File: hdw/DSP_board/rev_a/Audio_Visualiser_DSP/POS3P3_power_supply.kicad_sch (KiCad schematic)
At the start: 25 parts, among them Q401 BSS214NW, Q402 ZXMS6004FFTA, U401 74LVC1G97, U402 TPS62130A

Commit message: assigned many digi-key part numbers
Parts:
- C401, C406: Digi-Key PN (none) -> 1276-CL05B104KB5NNNCCT-ND
- C402, C404: Digi-Key PN (none) -> 1276-1075-1-ND
- C403, C407, C408: Digi-Key PN (none) -> 490-14381-1-ND
- C405: Digi-Key PN (none) -> 490-4516-1-ND
- R401, R406: Digi-Key PN (none) -> 311-0.0LRCT-ND
- R402, R403, R404: Digi-Key PN (none) -> 311-10.0KLRCT-ND
- R405, R408: Digi-Key PN (none) -> 311-10.0LRCT-ND
- R409: Digi-Key PN (none) -> 311-3.16KLRCT-ND
- R410: Digi-Key PN (none) -> 311-1.00KLRCT-ND
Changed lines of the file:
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@@
 			)
 		)
-		(property "Digi-Key PN" ""
+		(property "Digi-Key PN" "490-14381-1-ND"
 			(at 97.155 153.67 0)
 			(hide yes)
@@
 			)
 		)
-		(property "Digi-Key PN" ""
+		(property "Digi-Key PN" "311-10.0KLRCT-ND"
 			(at 78.74 78.74 0)
 			(hide yes)
@@
 			)
 		)
-		(property "Digi-Key PN" ""
+		(property "Digi-Key PN" "311-1.00KLRCT-ND"
 			(at 214.63 104.14 0)
 			(hide yes)
@@
 			)
 		)
-		(property "Digi-Key PN" ""
+		(property "Digi-Key PN" "311-10.0KLRCT-ND"
 			(at 55.88 104.14 0)
 			(hide yes)
@@
 			)
 		)
-		(property "Digi-Key PN" ""
+		(property "Digi-Key PN" "490-14381-1-ND"
 			(at 200.025 63.5 0)
 			(hide yes)
@@
 			)
 		)
-		(property "Digi-Key PN" ""
+		(property "Digi-Key PN" "311-3.16KLRCT-ND"
 			(at 222.25 88.9 0)
 			(hide yes)
@@
 			)
 		)
-		(property "Digi-Key PN" ""
+		(property "Digi-Key PN" "490-14381-1-ND"
 			(at 184.785 63.5 0)
 			(hide yes)
@@
 			)
 		)
-		(property "Digi-Key PN" ""
+		(property "Digi-Key PN" "1276-CL05B104KB5NNNCCT-ND"
 			(at 67.31 114.3 0)
 			(hide yes)
@@
 			)
 		)
-		(property "Digi-Key PN" ""
+		(property "Digi-Key PN" "1276-1075-1-ND"
 			(at 100.965 55.88 0)
 			(hide yes)
@@
 			)
 		)
-		(property "Digi-Key PN" ""
+		(property "Digi-Key PN" "1276-CL05B104KB5NNNCCT-ND"
 			(at 115.57 68.58 0)
 			(hide yes)
@@
 			)
 		)
-		(property "Digi-Key PN" ""
+		(property "Digi-Key PN" "311-0.0LRCT-ND"
 			(at 43.18 179.07 0)
 			(hide yes)
@@
 			)
 		)
-		(property "Digi-Key PN" ""
+		(property "Digi-Key PN" "1276-1075-1-ND"
 			(at 81.915 55.88 0)
 			(hide yes)
@@
 			)
 		)
-		(property "Digi-Key PN" ""
+		(property "Digi-Key PN" "311-10.0LRCT-ND"
 			(at 189.23 60.96 0)
 			(hide yes)
@@
 			)
 		)
-		(property "Digi-Key PN" ""
+		(property "Digi-Key PN" "311-0.0LRCT-ND"
 			(at 181.61 104.14 0)
 			(hide yes)
@@
 			)
 		)
-		(property "Digi-Key PN" ""
+		(property "Digi-Key PN" "311-10.0LRCT-ND"
 			(at 201.93 60.96 0)
 			(hide yes)
@@
 			)
 		)
-		(property "Digi-Key PN" ""
+		(property "Digi-Key PN" "311-10.0KLRCT-ND"
 			(at 111.76 156.21 0)
 			(hide yes)
@@
 			)
 		)
-		(property "Digi-Key PN" ""
+		(property "Digi-Key PN" "490-4516-1-ND"
 			(at 106.68 114.3 0)
 			(hide yes)

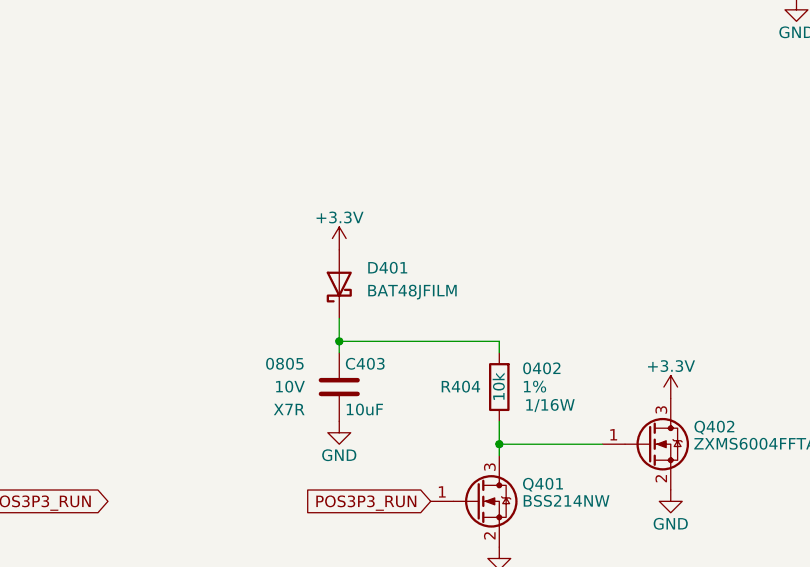
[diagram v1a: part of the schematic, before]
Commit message: Added a bunch of stuff to the schematic
Moved to adafruit I2C rotary encoder module. Added signal test points. Added some design schematic notes. Added LEd output connector ESD diodes. Consolidated on a single schottky diode. Connected most signals to MCU
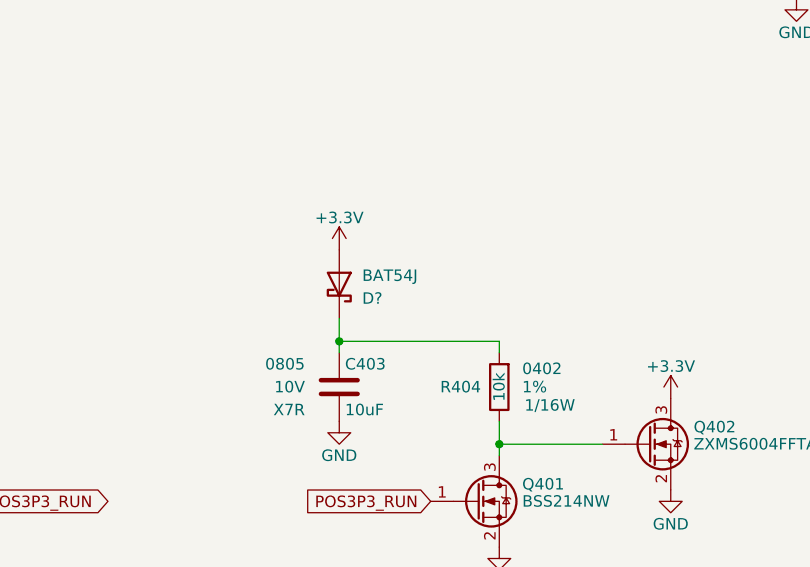
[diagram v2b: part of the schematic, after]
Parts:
- removed D401: BAT48JFILM, Diode_SMD:D_SOD-323, symbol Diode:BAT48JFILM
- added D?: BAT54J, Diode_SMD:D_SOD-323F, symbol Diode:BAT54J
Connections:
- net +3.3V: now also D?.2 (A)
- net at C403.1, R404.1: now also D?.1 (K)
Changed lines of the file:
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@@
-	)
-	(symbol
-		(lib_id "Diode:BAT48JFILM")
-		(at 86.36 154.94 90)
-		(unit 1)
-		(body_style 1)
-		(exclude_from_sim yes)
-		(in_bom yes)
-		(on_board yes)
-		(in_pos_files yes)
-		(dnp no)
-		(property "Reference" "D401"
-			(at 89.408 153.162 90)
-			(show_name no)
-			(do_not_autoplace no)
-			(effects
-				(font
-					(size 1.27 1.27)
-				)
-				(justify right)
-			)
-		)
-		(property "Value" "BAT48JFILM"
-			(at 89.408 155.702 90)
-			(show_name no)
-			(do_not_autoplace no)
-			(effects
-				(font
-					(size 1.27 1.27)
-				)
-				(justify right)
-			)
-		)
-		(property "Footprint" "Diode_SMD:D_SOD-323"
-			(at 90.805 154.94 0)
-			(hide yes)
-			(show_name no)
-			(do_not_autoplace no)
-			(effects
-				(font
-					(size 1.27 1.27)
-				)
-			)
-		)
-		(property "Datasheet" "www.st.com/resource/en/datasheet/bat48.pdf"
-			(at 86.36 154.94 0)
-			(hide yes)
-			(show_name no)
-			(do_not_autoplace no)
-			(effects
-				(font
-					(size 1.27 1.27)
-				)
-			)
-		)
-		(property "Description" ""
-			(at 86.36 154.94 0)
-			(hide yes)
-			(show_name no)
-			(do_not_autoplace no)
-			(effects
-				(font
-					(size 1.27 1.27)
-				)
-			)
-		)
-		(property "Digi-Key PN" "497-5711-1-ND"
-			(at 86.36 154.94 0)
-			(hide yes)
-			(show_name no)
-			(do_not_autoplace no)
-			(effects
-				(font
-					(size 1.27 1.27)
-				)
-			)
-		)
-		(property "Sim.Type" ""
-			(at 86.36 154.94 90)
-			(hide yes)
-			(show_name no)
-			(do_not_autoplace no)
-			(effects
-				(font
-					(size 1.27 1.27)
-				)
-			)
-		)
-		(pin "1"
-		)
-		(pin "2"
-		)
-		(instances
-			(project "Audio_Visualiser_DSP"
-				(path "/97a4dfb8-0e16-46f1-9709-8d2007dd0cd3/b2362e66-49f5-4e26-9e9f-2de376dec3c9"
-					(reference "D401")
-					(unit 1)
-				)
-			)
-		)
 	)
 	(symbol
@@
 					(unit 1)
 				)
+			)
+		)
+	)
+	(symbol
+		(lib_id "Diode:BAT54J")
+		(at 86.36 154.94 270)
+		(mirror x)
+		(unit 1)
+		(body_style 1)
+		(exclude_from_sim no)
+		(in_bom yes)
+		(on_board yes)
+		(in_pos_files yes)
+		(dnp no)
+		(property "Reference" "D?"
+			(at 88.9 156.5276 90)
+			(show_name no)
+			(do_not_autoplace no)
+			(effects
+				(font
+					(size 1.27 1.27)
+				)
+				(justify left)
+			)
+		)
+		(property "Value" "BAT54J"
+			(at 88.9 153.9876 90)
+			(show_name no)
+			(do_not_autoplace no)
+			(effects
+				(font
+					(size 1.27 1.27)
+				)
+				(justify left)
+			)
+		)
+		(property "Footprint" "Diode_SMD:D_SOD-323F"
+			(at 81.915 154.94 0)
+			(hide yes)
+			(show_name no)
+			(do_not_autoplace no)
+			(effects
+				(font
+					(size 1.27 1.27)
+				)
+			)
+		)
+		(property "Datasheet" "https://assets.nexperia.com/documents/data-sheet/BAT54J.pdf"
+			(at 86.36 154.94 0)
+			(hide yes)
+			(show_name no)
+			(do_not_autoplace no)
+			(effects
+				(font
+					(size 1.27 1.27)
+				)
+			)
+		)
+		(property "Description" "30V 200mA Schottky diode, SOD-323F"
+			(at 86.36 154.94 0)
+			(hide yes)
+			(show_name no)
+			(do_not_autoplace no)
+			(effects
+				(font
+					(size 1.27 1.27)
+				)
+			)
+		)
+		(property "Sim.Library" "C:\\Users\\drewm\\Documents\\KiCad Projects\\Projects\\audio_visualiser\\hdw\\DSP_board\\rev_a\\sim\\spice_models\\BAT54SW.lib"
+			(at 86.36 154.94 0)
+			(hide yes)
+			(show_name no)
+			(do_not_autoplace no)
+			(effects
+				(font
+					(size 1.27 1.27)
+				)
+			)
+		)
+		(property "Sim.Name" "BAT54SW"
+			(at 86.36 154.94 0)
+			(hide yes)
+			(show_name no)
+			(do_not_autoplace no)
+			(effects
+				(font
+					(size 1.27 1.27)
+				)
+			)
+		)
+		(property "Sim.Device" "SUBCKT"
+			(at 86.36 154.94 0)
+			(hide yes)
+			(show_name no)
+			(do_not_autoplace no)
+			(effects
+				(font
+					(size 1.27 1.27)
+				)
+			)
+		)
+		(property "Sim.Pins" "1=2 2=1"
+			(at 86.36 154.94 0)
+			(hide yes)
+			(show_name no)
+			(do_not_autoplace no)
+			(effects
+				(font
+					(size 1.27 1.27)
+				)
+			)
+		)
+		(pin "2"
+		)
+		(pin "1"
+		)
+		(instances
+			(project "Audio_Visualiser_DSP"
+				(path "/97a4dfb8-0e16-46f1-9709-8d2007dd0cd3/b2362e66-49f5-4e26-9e9f-2de376dec3c9"
+					(reference "D?")
+					(unit 1)
+				)

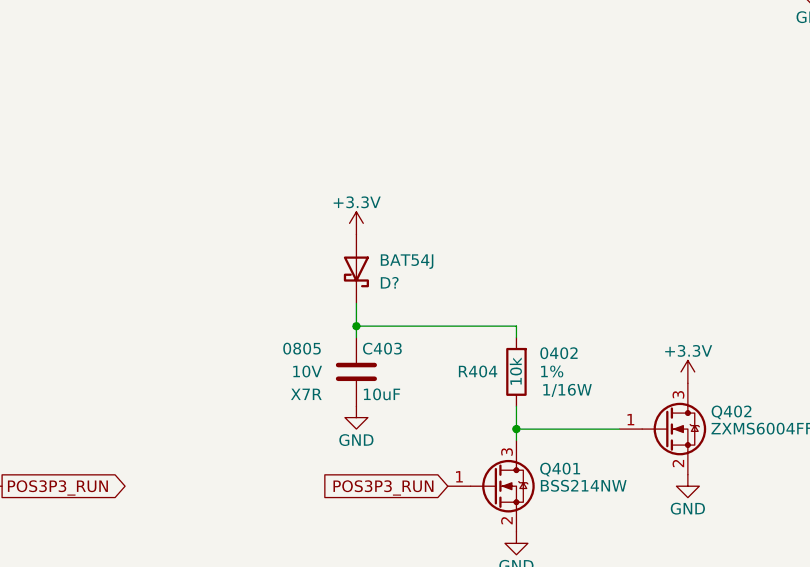
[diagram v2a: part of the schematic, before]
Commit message: Added simulation outputs, sim readme
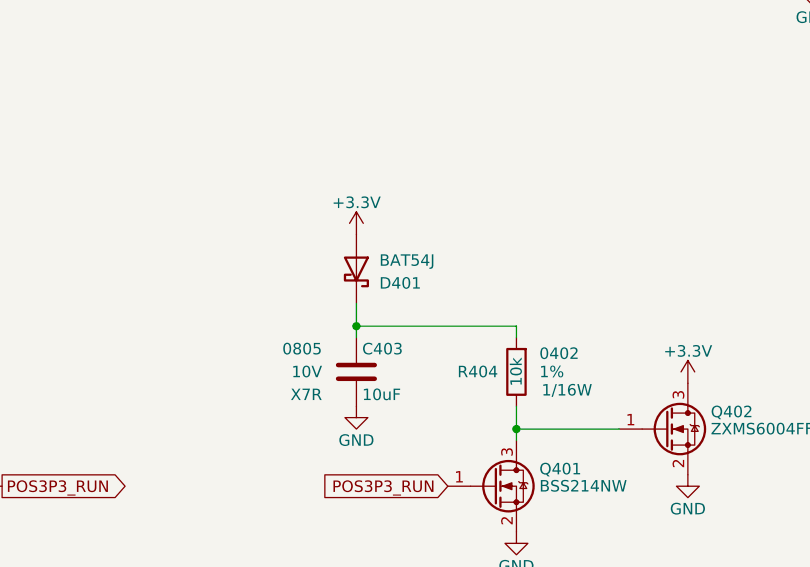
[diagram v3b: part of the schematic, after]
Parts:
- gave numbers to parts that had none: 1
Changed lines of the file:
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@@
 		(in_pos_files yes)
 		(dnp no)
-		(property "Reference" "D?"
+		(property "Reference" "D401"
 			(at 88.9 156.5276 90)
 			(show_name no)
@@
 			(project "Audio_Visualiser_DSP"
 				(path "/97a4dfb8-0e16-46f1-9709-8d2007dd0cd3/b2362e66-49f5-4e26-9e9f-2de376dec3c9"
-					(reference "D?")
+					(reference "D401")
 					(unit 1)
 				)

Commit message: Defined legit KiCad BOM variants
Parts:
- R405, R408: now not fitted
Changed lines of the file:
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@@
 					(reference "C403")
 					(unit 1)
+					(variant
+						(name "Default")
+					)
+					(variant
+						(name "Development")
+					)
 				)
 			)
@@
 					(reference "R403")
 					(unit 1)
+					(variant
+						(name "Default")
+					)
+					(variant
+						(name "Development")
+					)
 				)
 			)
@@
 					(reference "R410")
 					(unit 1)
+					(variant
+						(name "Default")
+					)
+					(variant
+						(name "Development")
+					)
 				)
 			)
@@
 					(reference "U402")
 					(unit 1)
+					(variant
+						(name "Default")
+					)
+					(variant
+						(name "Development")
+					)
 				)
 			)
@@
 					(reference "R402")
 					(unit 1)
+					(variant
+						(name "Default")
+					)
+					(variant
+						(name "Development")
+					)
 				)
 			)
@@
 					(reference "C408")
 					(unit 1)
+					(variant
+						(name "Default")
+					)
+					(variant
+						(name "Development")
+					)
 				)
 			)
@@
 					(reference "R409")
 					(unit 1)
+					(variant
+						(name "Default")
+					)
+					(variant
+						(name "Development")
+					)
 				)
 			)
@@
 					(reference "C407")
 					(unit 1)
+					(variant
+						(name "Default")
+					)
+					(variant
+						(name "Development")
+					)
 				)
 			)
@@
 					(reference "L401")
 					(unit 1)
+					(variant
+						(name "Default")
+					)
+					(variant
+						(name "Development")
+					)
 				)
 			)
@@
 					(reference "U401")
 					(unit 1)
+					(variant
+						(name "Default")
+					)
+					(variant
+						(name "Development")
+					)
 				)
 			)
@@
 					(reference "C401")
 					(unit 1)
+					(variant
+						(name "Default")
+					)
+					(variant
+						(name "Development")
+					)
 				)
 			)
@@
 					(reference "C404")
 					(unit 1)
+					(variant
+						(name "Default")
+					)
+					(variant
+						(name "Development")
+					)
 				)
 			)
@@
 					(reference "C406")
 					(unit 1)
+					(variant
+						(name "Default")
+					)
+					(variant
+						(name "Development")
+					)
 				)
 			)
@@
 					(reference "R401")
 					(unit 1)
+					(variant
+						(name "Default")
+					)
+					(variant
+						(name "Development")
+					)
 				)
 			)
@@
 					(reference "C402")
 					(unit 1)
+					(variant
+						(name "Default")
+					)
+					(variant
+						(name "Development")
+					)
 				)
 			)
@@
 		(on_board yes)
 		(in_pos_files yes)
-		(dnp no)
+		(dnp yes)
 		(property "Reference" "R405"
 			(at 191.77 60.96 90)
@@
 					(reference "R405")
 					(unit 1)
+					(variant
+						(name "Default")
+					)
+					(variant
+						(name "Development")
+						(dnp no)
+					)
 				)
 			)
@@
 					(reference "R407")
 					(unit 1)
+					(variant
+						(name "Default")
+					)
+					(variant
+						(name "Development")
+					)
 				)
 			)
@@
 					(reference "D401")
 					(unit 1)
+					(variant
+						(name "Default")
+					)
+					(variant
+						(name "Development")
+					)
 				)
 			)
@@
 					(reference "R406")
 					(unit 1)
+					(variant
+						(name "Default")
+					)
+					(variant
+						(name "Development")
+					)
 				)
 			)
@@
 					(reference "TP401")
 					(unit 1)
+					(variant
+						(name "Default")
+					)
+					(variant
+						(name "Development")
+					)
 				)
 			)
@@
 		(on_board yes)
 		(in_pos_files yes)
-		(dnp no)
+		(dnp yes)
 		(property "Reference" "R408"
 			(at 204.47 60.96 90)
@@
 					(reference "R408")
 					(unit 1)
+					(variant
+						(name "Default")
+					)
+					(variant
+						(name "Development")
+						(dnp no)
+					)
 				)
 			)
@@
 					(reference "R404")
 					(unit 1)
+					(variant
+						(name "Default")
+					)
+					(variant
+						(name "Development")
+					)
 				)
 			)
@@
 					(reference "C405")
 					(unit 1)
+					(variant
+						(name "Default")
+					)
+					(variant
+						(name "Development")
+					)
 				)
 			)
@@
 					(reference "Q402")
 					(unit 1)
+					(variant
+						(name "Default")
+					)
+					(variant
+						(name "Development")
+					)
 				)
 			)
@@
 					(reference "Q401")
 					(unit 1)
+					(variant
+						(name "Default")
+					)
+					(variant
+						(name "Development")
+					)
 				)
 			)
